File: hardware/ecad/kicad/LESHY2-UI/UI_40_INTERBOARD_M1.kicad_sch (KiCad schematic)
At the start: 0 parts

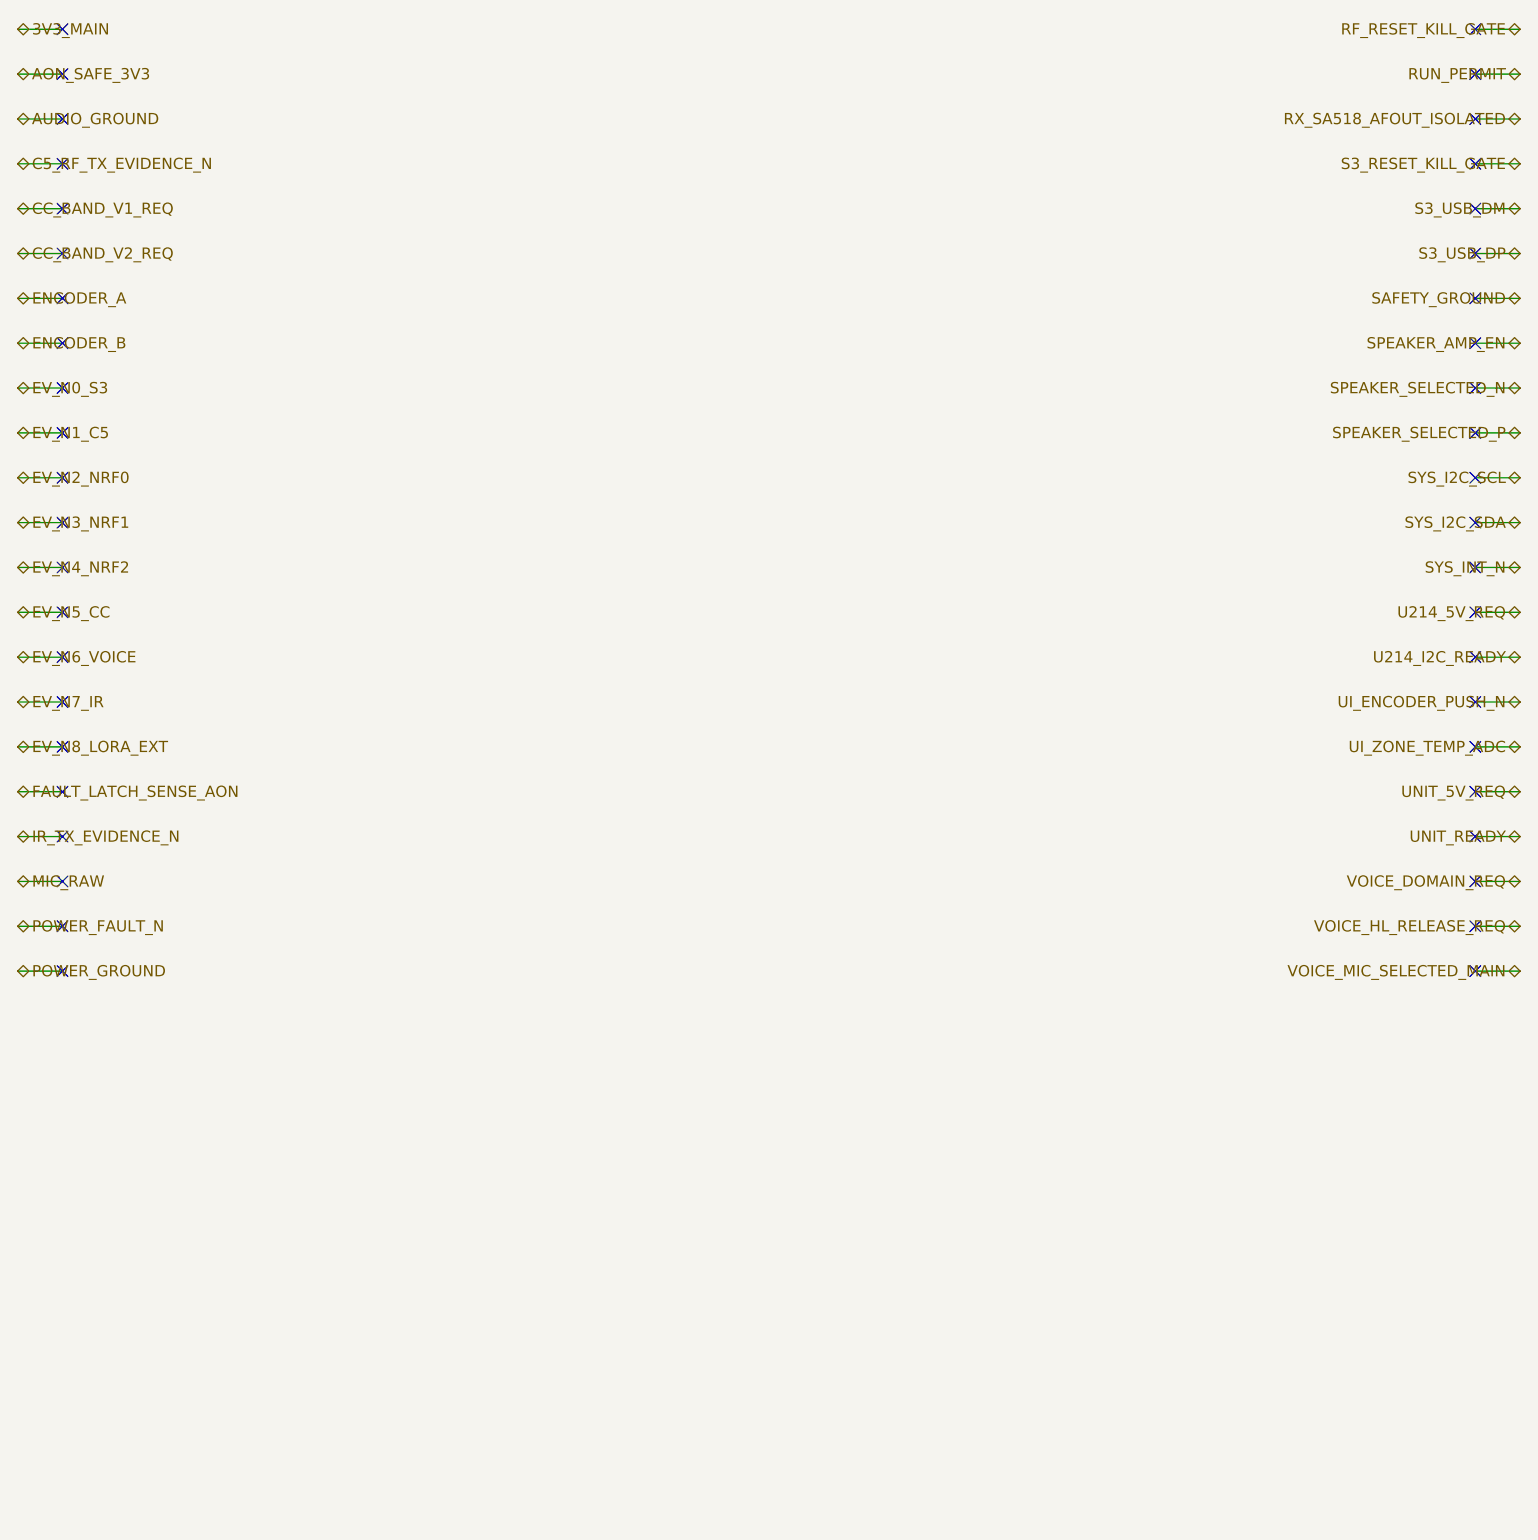
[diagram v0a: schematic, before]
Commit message: Complete H2.2.2 S3 core schematic
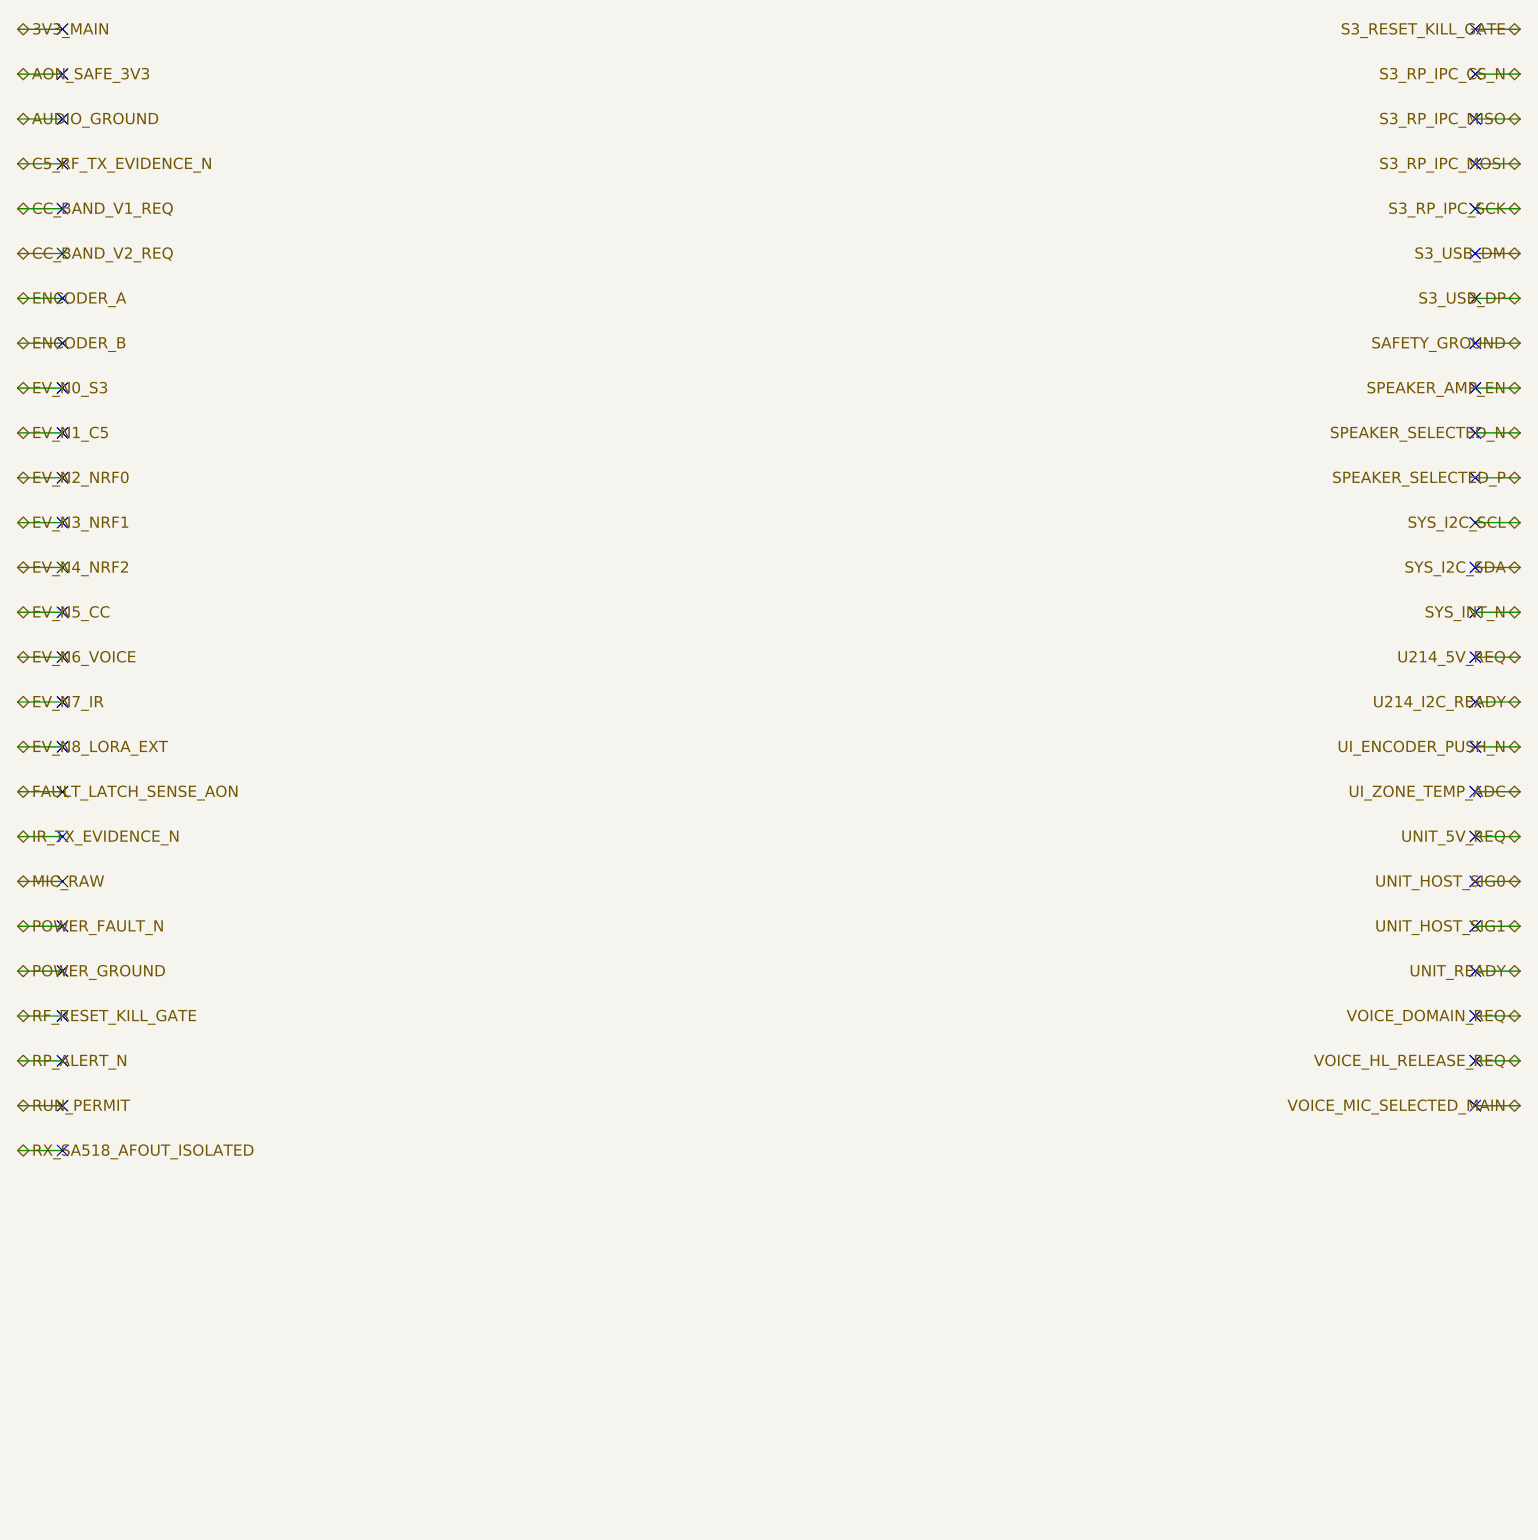
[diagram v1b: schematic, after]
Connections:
- no-connect marks 44 -> 51

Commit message: complete exact H2.2.8 UI interboard schematic
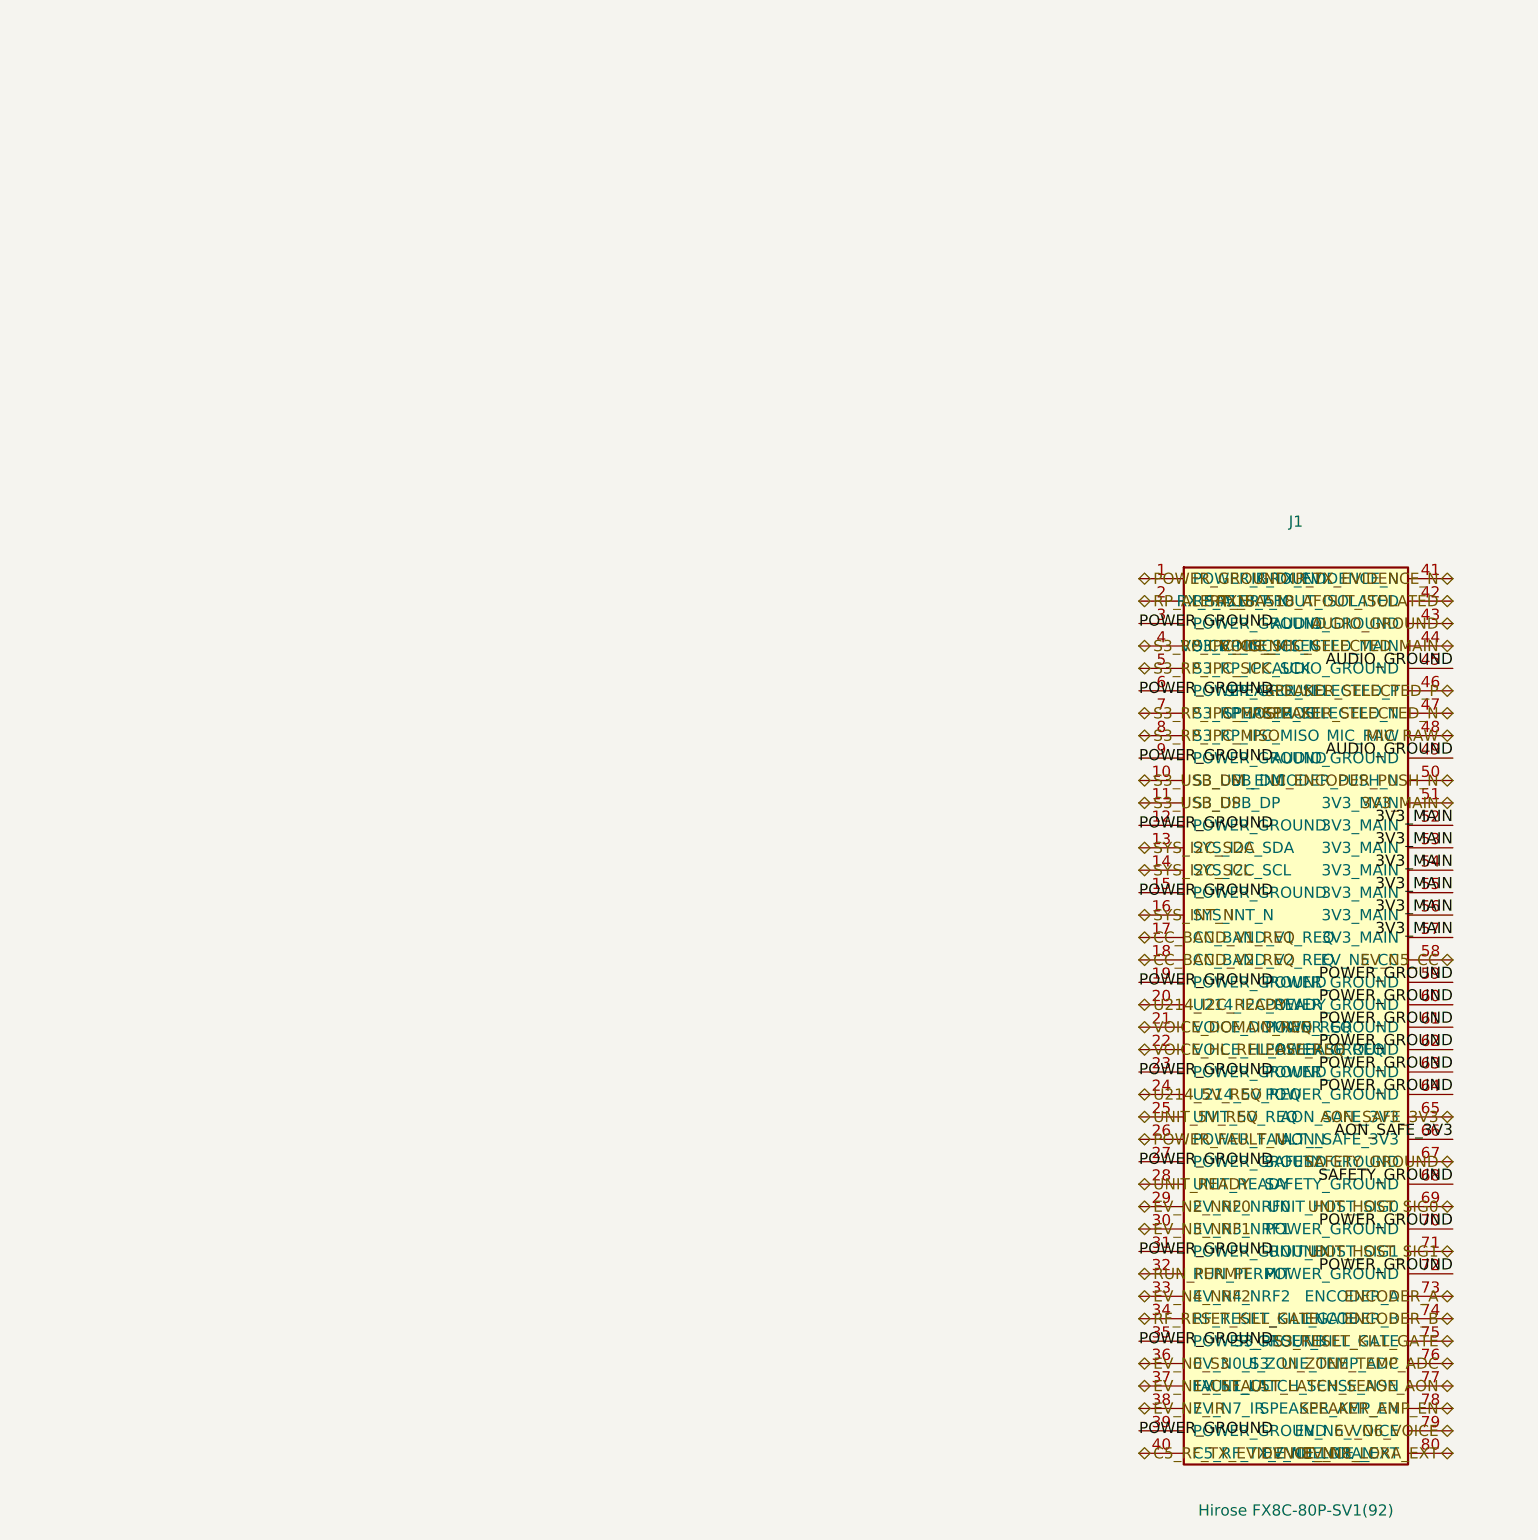
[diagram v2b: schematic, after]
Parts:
- added J1: Hirose FX8C-80P-SV1(92), Connector_Hirose_FX8:Hirose_FX8-80P-SV_2x40_P0.6mm, symbol Leshy2:UI40_M1_UI_PLUG
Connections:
- net 3V3_MAIN: now also J1.51 (3V3_MAIN), J1.52 (3V3_MAIN), J1.53 (3V3_MAIN), J1.54 (3V3_MAIN), J1.55 (3V3_MAIN), J1.56 (3V3_MAIN), J1.57 (3V3_MAIN)
- net AON_SAFE_3V3: now also J1.65 (AON_SAFE_3V3), J1.66 (AON_SAFE_3V3)
- net AUDIO_GROUND: now also J1.43 (AUDIO_GROUND), J1.45 (AUDIO_GROUND), J1.49 (AUDIO_GROUND)
- net C5_RF_TX_EVIDENCE_N: now also J1.40 (C5_RF_TX_EVIDENCE_N)
- net CC_BAND_V1_REQ: now also J1.17 (CC_BAND_V1_REQ)
- net CC_BAND_V2_REQ: now also J1.18 (CC_BAND_V2_REQ)
- net ENCODER_A: now also J1.73 (ENCODER_A)
- net ENCODER_B: now also J1.74 (ENCODER_B)
- net EV_N0_S3: now also J1.36 (EV_N0_S3)
- net EV_N1_C5: now also J1.37 (EV_N1_C5)
- net EV_N2_NRF0: now also J1.29 (EV_N2_NRF0)
- net EV_N3_NRF1: now also J1.30 (EV_N3_NRF1)
- net EV_N4_NRF2: now also J1.33 (EV_N4_NRF2)
- net EV_N5_CC: now also J1.58 (EV_N5_CC)
- net EV_N6_VOICE: now also J1.79 (EV_N6_VOICE)
- net EV_N7_IR: now also J1.38 (EV_N7_IR)
- net EV_N8_LORA_EXT: now also J1.80 (EV_N8_LORA_EXT)
- net FAULT_LATCH_SENSE_AON: now also J1.77 (FAULT_LATCH_SENSE_AON)
- net IR_TX_EVIDENCE_N: now also J1.41 (IR_TX_EVIDENCE_N)
- net MIC_RAW: now also J1.48 (MIC_RAW)
- net POWER_FAULT_N: now also J1.26 (POWER_FAULT_N)
- net POWER_GROUND: now also J1.1 (POWER_GROUND), J1.12 (POWER_GROUND), J1.15 (POWER_GROUND), J1.19 (POWER_GROUND), J1.23 (POWER_GROUND), J1.27 (POWER_GROUND), J1.3 (POWER_GROUND), J1.31 (POWER_GROUND), J1.35 (POWER_GROUND), J1.39 (POWER_GROUND), J1.59 (POWER_GROUND), J1.6 (POWER_GROUND), J1.60 (POWER_GROUND), J1.61 (POWER_GROUND), J1.62 (POWER_GROUND), J1.63 (POWER_GROUND), J1.64 (POWER_GROUND), J1.70 (POWER_GROUND), J1.72 (POWER_GROUND), J1.9 (POWER_GROUND)
- net RF_RESET_KILL_GATE: now also J1.34 (RF_RESET_KILL_GATE)
- net RP_ALERT_N: now also J1.2 (RP_ALERT_N)
- net RUN_PERMIT: now also J1.32 (RUN_PERMIT)
- net RX_SA518_AFOUT_ISOLATED: now also J1.42 (RX_SA518_AFOUT_ISOLATED)
- net S3_RESET_KILL_GATE: now also J1.75 (S3_RESET_KILL_GATE)
- net S3_RP_IPC_CS_N: now also J1.4 (S3_RP_IPC_CS_N)
- net S3_RP_IPC_MISO: now also J1.8 (S3_RP_IPC_MISO)
- net S3_RP_IPC_MOSI: now also J1.7 (S3_RP_IPC_MOSI)
- net S3_RP_IPC_SCK: now also J1.5 (S3_RP_IPC_SCK)
- net S3_USB_DM: now also J1.10 (S3_USB_DM)
- net S3_USB_DP: now also J1.11 (S3_USB_DP)
- net SAFETY_GROUND: now also J1.67 (SAFETY_GROUND), J1.68 (SAFETY_GROUND)
- net SPEAKER_AMP_EN: now also J1.78 (SPEAKER_AMP_EN)
- net SPEAKER_SELECTED_N: now also J1.47 (SPEAKER_SELECTED_N)
- net SPEAKER_SELECTED_P: now also J1.46 (SPEAKER_SELECTED_P)
- net SYS_I2C_SCL: now also J1.14 (SYS_I2C_SCL)
- net SYS_I2C_SDA: now also J1.13 (SYS_I2C_SDA)
- net SYS_INT_N: now also J1.16 (SYS_INT_N)
- net U214_5V_REQ: now also J1.24 (U214_5V_REQ)
- net U214_I2C_READY: now also J1.20 (U214_I2C_READY)
- net UI_ENCODER_PUSH_N: now also J1.50 (UI_ENCODER_PUSH_N)
- net UI_ZONE_TEMP_ADC: now also J1.76 (UI_ZONE_TEMP_ADC)
- net UNIT_5V_REQ: now also J1.25 (UNIT_5V_REQ)
- net UNIT_HOST_SIG0: now also J1.69 (UNIT_HOST_SIG0)
- net UNIT_HOST_SIG1: now also J1.71 (UNIT_HOST_SIG1)
- net UNIT_READY: now also J1.28 (UNIT_READY)
- net VOICE_DOMAIN_REQ: now also J1.21 (VOICE_DOMAIN_REQ)
- net VOICE_HL_RELEASE_REQ: now also J1.22 (VOICE_HL_RELEASE_REQ)
- net VOICE_MIC_SELECTED_MAIN: now also J1.44 (VOICE_MIC_SELECTED_MAIN)
- no-connect marks 51 -> 0
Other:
- title: (none) -> Leshy2 — exact UI-side 80-contact M1 plug

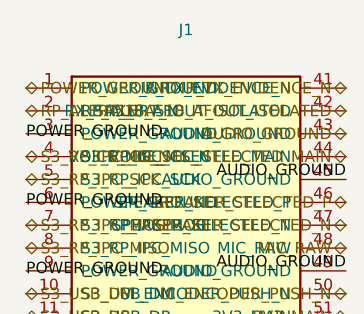
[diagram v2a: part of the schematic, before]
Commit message: complete H2 schematic review package
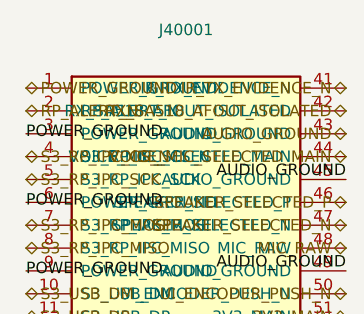
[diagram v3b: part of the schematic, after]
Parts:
- renumbered J1 to J40001
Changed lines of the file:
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@@
 		(on_board yes)
 		(dnp no)
-		(property "Reference" "J1"
+		(property "Reference" "J40001"
 			(at 165.10 76.08 0)
 			(show_name no)
@@
 			(project "LESHY2-UI"
 				(path "/d200dfe6-1a3a-53e5-9a6e-136dec8498dd"
-					(reference "J1")
+					(reference "J40001")
 					(unit 1)
 				)

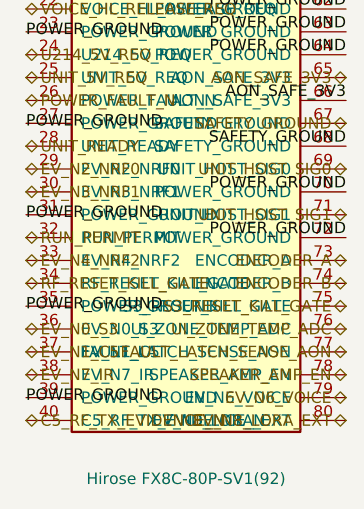
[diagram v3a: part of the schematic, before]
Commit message: review H3.6.2 single-fault containment
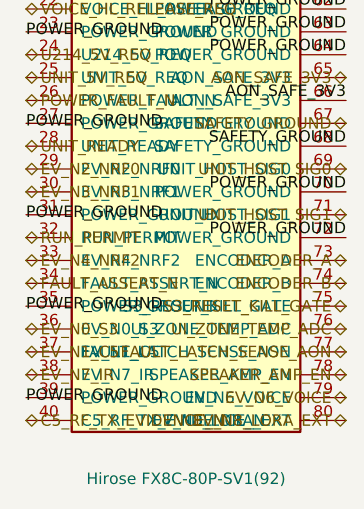
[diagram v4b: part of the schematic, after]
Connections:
- net RF_RESET_KILL_GATE renamed FAULT_ASSERT_N
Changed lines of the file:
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@@
 		(effects (font (size 1.27 1.27)))
 	)
-	(hierarchical_label "RF_RESET_KILL_GATE"
+	(hierarchical_label "FAULT_ASSERT_N"
 		(shape bidirectional)
 		(at 147.32 166.37 0)

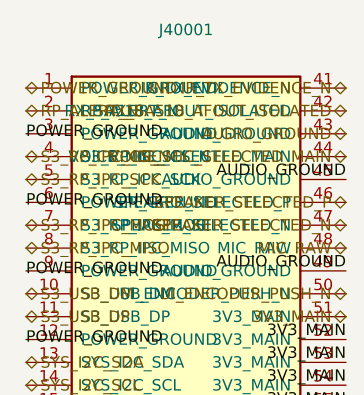
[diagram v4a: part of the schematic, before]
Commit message: Reclose H2 through H4 on dual SA818S architecture
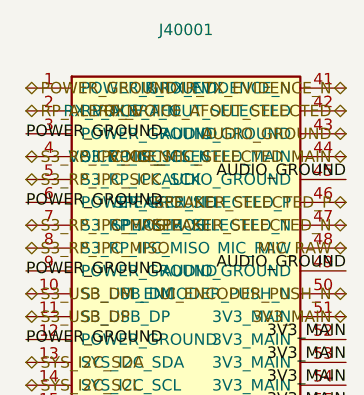
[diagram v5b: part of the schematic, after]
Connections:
- net RX_SA518_AFOUT_ISOLATED renamed RX_VOICE_AFOUT_SELECTED
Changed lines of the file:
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@@
 		(effects (font (size 1.27 1.27)) (justify right bottom))
 	)
-	(hierarchical_label "RX_SA518_AFOUT_ISOLATED"
+	(hierarchical_label "RX_VOICE_AFOUT_SELECTED"
 		(shape bidirectional)
 		(at 182.88 85.09 180)
